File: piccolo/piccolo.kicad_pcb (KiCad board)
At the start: 2 copper layers, 136.6 x 20.6 mm, 21 parts, among them U1 ProMicro

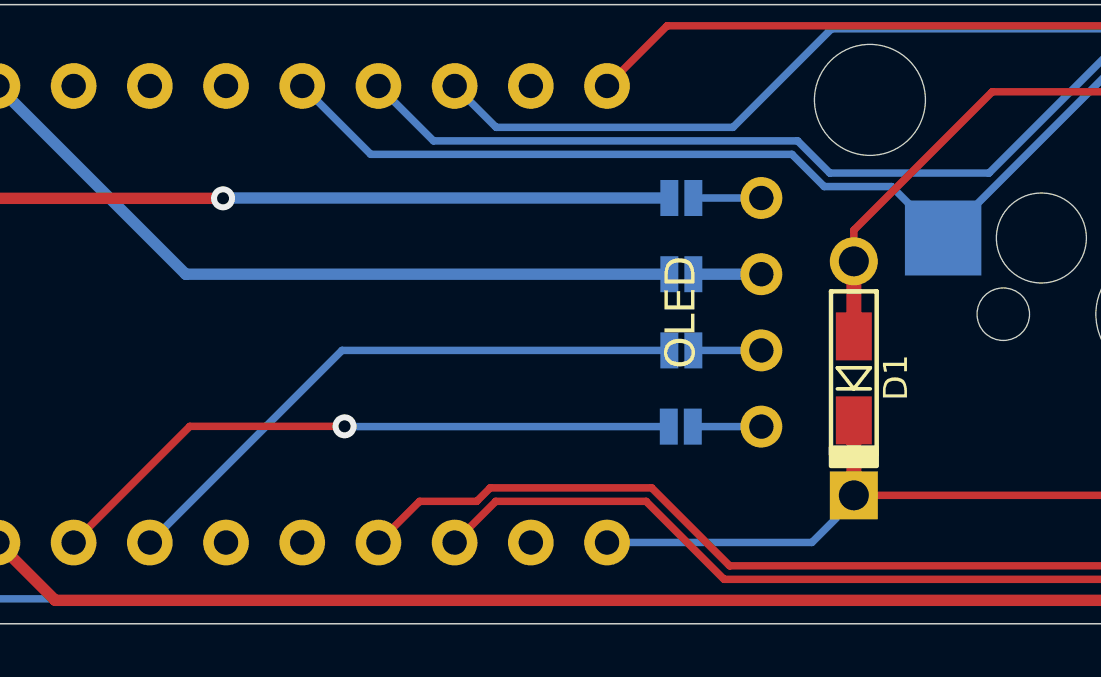
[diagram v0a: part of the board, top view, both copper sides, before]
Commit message: make oled cutout larger in switchplate.  Prepare rev3 gerbers
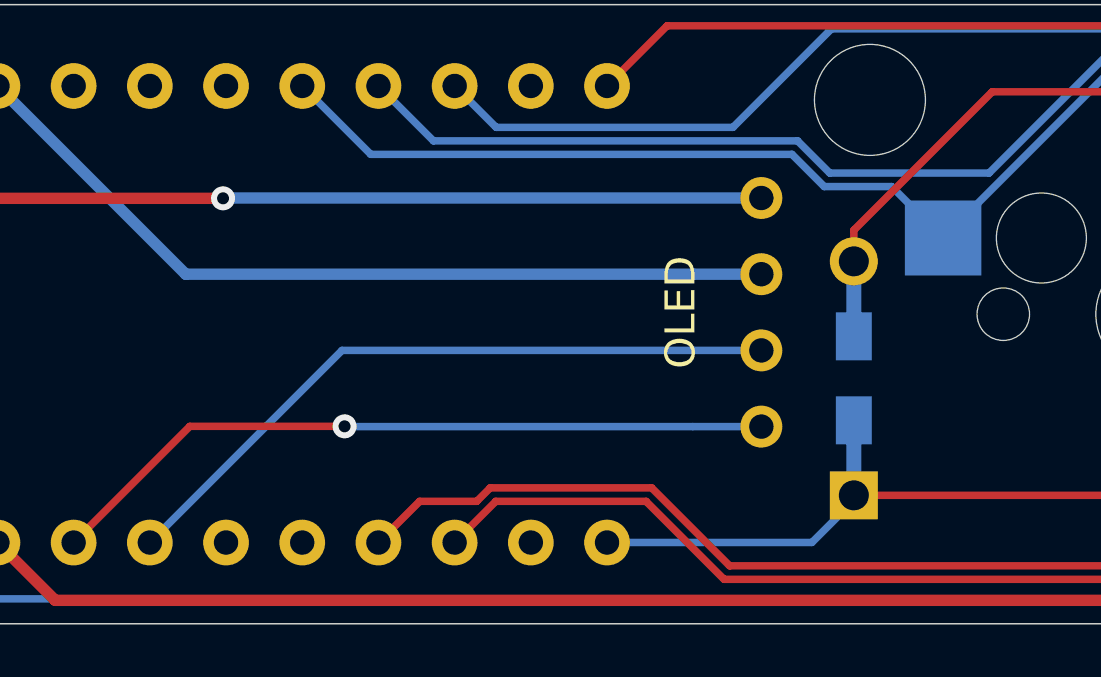
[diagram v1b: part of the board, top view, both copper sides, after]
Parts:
- removed GND1, SCL1, SDA1, VCC1: SolderJumper_2_Open, Keyboard parts:SOLDER_JUMPER_2
- D1: moved to F.Cu
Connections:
- OL1 pad 1: Net-(OL1-Pad1) -> SDA
- OL1 pad 2: Net-(OL1-Pad2) -> SCL
- OL1 pad 3: Net-(OL1-Pad3) -> VCC
- OL1 pad 4: Net-(GND1-Pad2) -> GND
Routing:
- net GND: track 177.1 -> 182.5 mm
- net SDA: track 21.4 -> 24.5 mm
- net VCC: track 25.0 -> 28.1 mm
- net SCL: track 20.0 -> 23.0 mm
- net Net-(OL1-Pad1): track 2.29 -> 0.00 mm
- net Net-(OL1-Pad3): track 2.27 -> 0.00 mm
- net Net-(OL1-Pad2): track 2.27 -> 0.00 mm
- net Net-(GND1-Pad2): track 2.27 -> 0.00 mm
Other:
- board text added: "Piccolo Macro Pad by JeJeff rev 0.3"
- board text removed: "Piccolo Macro Pad by JeJeff rev 0.2"

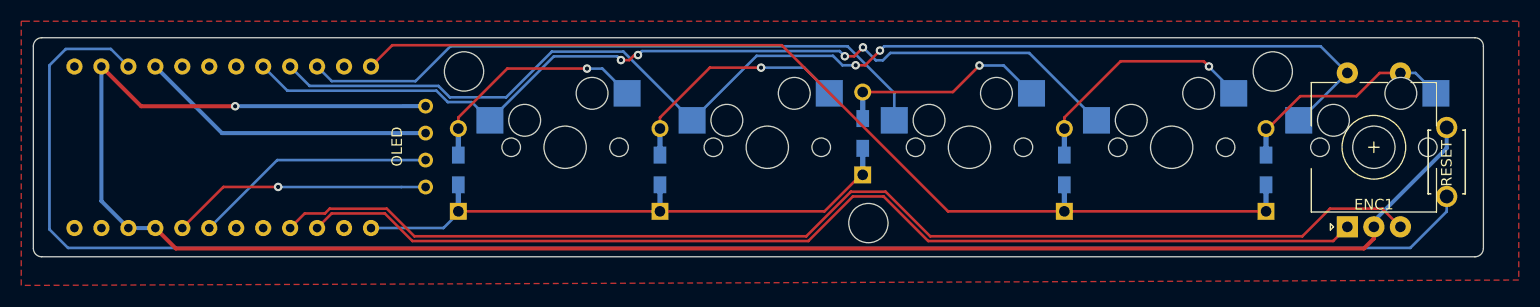
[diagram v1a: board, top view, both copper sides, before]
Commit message: Made the oled cutout larger. because the pins interfere with the switchplate.  Bump rev to 0.4
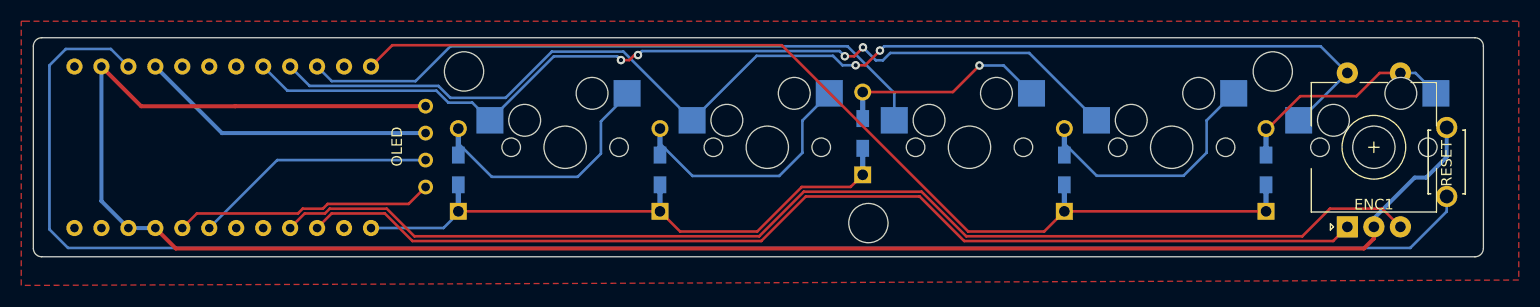
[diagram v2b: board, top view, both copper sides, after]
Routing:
- net Net-(D1-Pad2): track 19.8 -> 22.3 mm, vias 1 -> 0
- net Net-(D2-Pad2): track 20.0 -> 22.2 mm, vias 1 -> 0
- net Net-(D4-Pad2): track 20.6 -> 22.2 mm, vias 1 -> 0
- net GND: track 182.5 -> 180.8 mm, vias 1 -> 0
- net row1: track 91.6 -> 93.2 mm
- net row0: track 48.3 -> 49.9 mm
- net SDA: vias 1 -> 0
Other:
- board text added: "Piccolo Macro Pad by JeJeff rev 0.4"
- board text removed: "Piccolo Macro Pad by JeJeff rev 0.3"
